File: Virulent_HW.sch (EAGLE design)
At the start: 28 parts

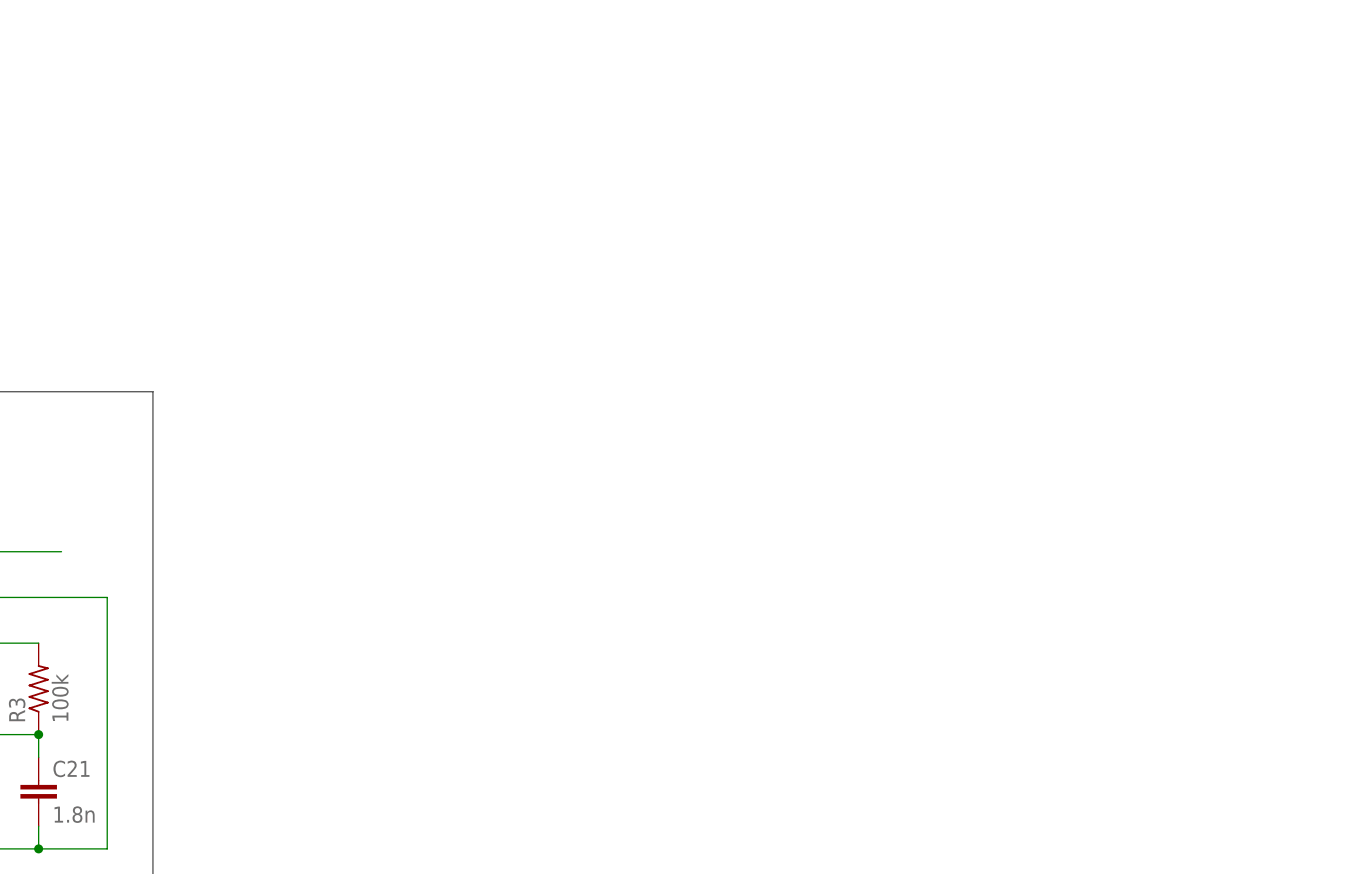
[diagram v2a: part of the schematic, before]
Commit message: Added crystal oscillator to library. Added carrier frequency circuitry to schematic.
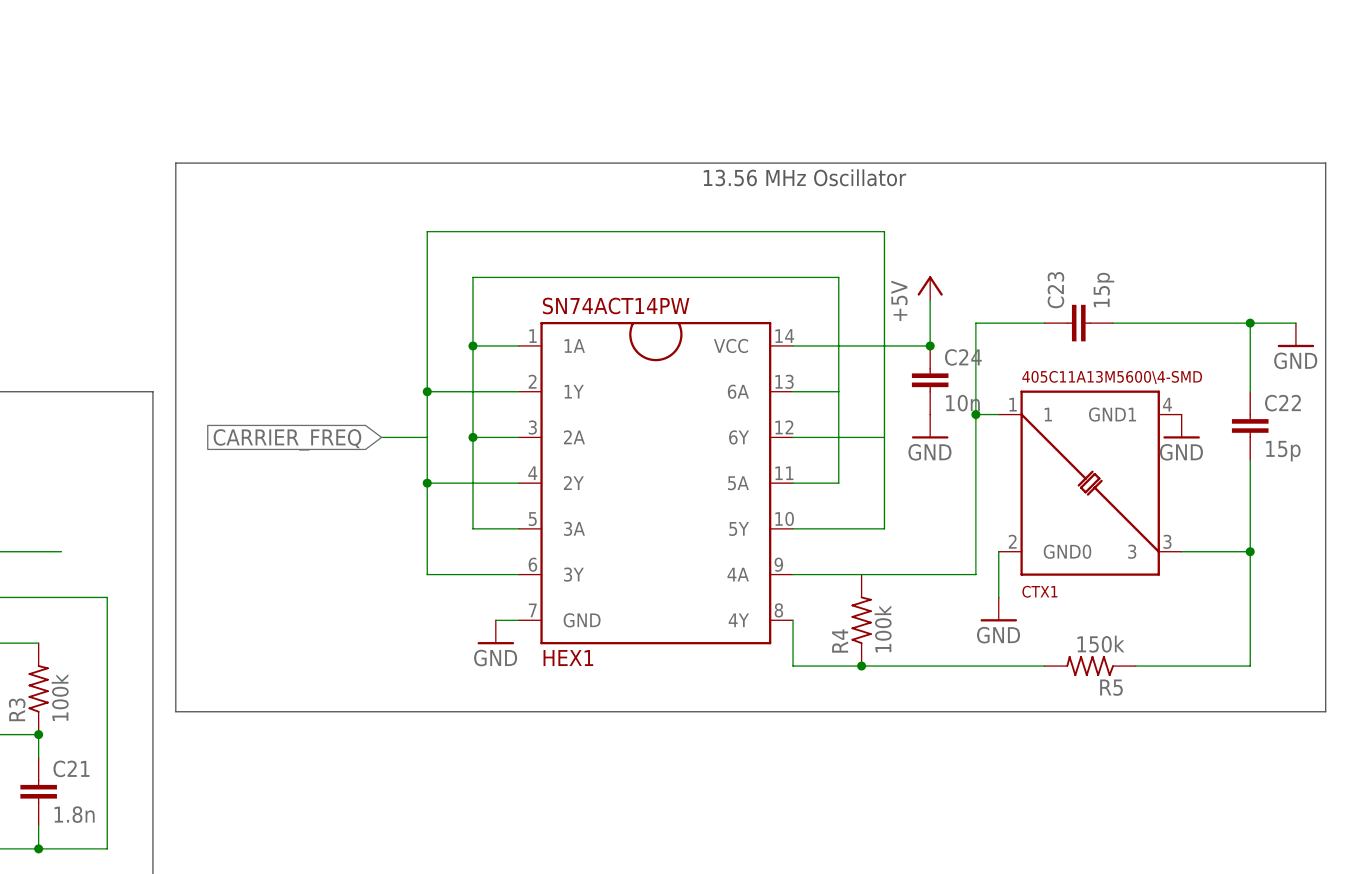
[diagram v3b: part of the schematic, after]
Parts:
- added C22, C23: 15p, rcl:C-EUC1206
- added C24: 10n, rcl:C-EUC1206
- added CTX1: 405C11A13M5600\4-SMD, Virulent_HW:405C11A13M5600\4-SMD
- added HEX1: SN74ACT14PW, Virulent_HW:SN74ACT14PW
- added R4: 100k, Virulent_HW:R-US_R0402
- added R5: 150k, Virulent_HW:R-US_R0402
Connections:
- new net CARRIER_FREQ: HEX1.1Y@2, HEX1.2Y@4, HEX1.3Y@6, HEX1.5Y@10, HEX1.6Y@12
- new net N$18: C23.1, CTX1.1@1, HEX1.4A@9, R4.2
- new net N$19: HEX1.4Y@8, R4.1, R5.2
- new net N$20: C22.2, CTX1.3@3, R5.1
- new net N$24: HEX1.1A@1, HEX1.2A@3, HEX1.3A@5, HEX1.5A@11, HEX1.6A@13
- net +5V: now also C24.1, HEX1.VCC@14
- net GND: now also C22.1, C23.2, C24.2, CTX1.GND0@2, CTX1.GND1@4, HEX1.GND@7
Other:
- note added: "13.56 MHz Oscillator"
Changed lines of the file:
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@@
 <part name="R3" library="Virulent_HW" deviceset="R-US_" device="R0402" value="100k"/>
 <part name="P+8" library="Virulent_HW" deviceset="+5V" device=""/>
+<part name="HEX1" library="Virulent_HW" deviceset="SN74ACT14" device="PW"/>
+<part name="CTX1" library="Virulent_HW" deviceset="405C11A13M5600" device="\4-SMD"/>
+<part name="GND9" library="Virulent_HW" deviceset="GND" device=""/>
+<part name="GND10" library="Virulent_HW" deviceset="GND" device=""/>
+<part name="R4" library="Virulent_HW" deviceset="R-US_" device="R0402" value="100k"/>
+<part name="R5" library="Virulent_HW" deviceset="R-US_" device="R0402" value="150k"/>
+<part name="C22" library="rcl" deviceset="C-EU" device="C1206" value="15p"/>
+<part name="C23" library="rcl" deviceset="C-EU" device="C1206" value="15p"/>
+<part name="GND11" library="Virulent_HW" deviceset="GND" device=""/>
+<part name="C24" library="rcl" deviceset="C-EU" device="C1206" value="10n"/>
+<part name="GND12" library="Virulent_HW" deviceset="GND" device=""/>
+<part name="P+9" library="Virulent_HW" deviceset="+5V" device=""/>
+<part name="GND13" library="Virulent_HW" deviceset="GND" device=""/>
 </parts>
 <sheets>
@@
 <wire x1="187.96" y1="71.12" x2="101.6" y2="71.12" width="0.1524" layer="97"/>
 <wire x1="101.6" y1="71.12" x2="101.6" y2="12.7" width="0.1524" layer="97"/>
+<wire x1="281.94" y1="96.52" x2="281.94" y2="35.56" width="0.1524" layer="97"/>
+<wire x1="281.94" y1="35.56" x2="409.702" y2="35.56" width="0.1524" layer="97"/>
+<wire x1="409.702" y1="35.56" x2="409.702" y2="96.52" width="0.1524" layer="97"/>
+<wire x1="409.702" y1="96.52" x2="281.94" y2="96.52" width="0.1524" layer="97"/>
+<text x="340.36" y="93.98" size="1.778" layer="97">13.56 MHz Oscillator</text>
 </plain>
 <instances>
@@
 <instance part="R3" gate="G$1" x="266.7" y="38.1" rot="R90"/>
 <instance part="P+8" gate="1" x="210.82" y="38.1" rot="R90"/>
+<instance part="HEX1" gate="G$1" x="335.28" y="60.96"/>
+<instance part="CTX1" gate="G$1" x="383.54" y="60.96"/>
+<instance part="GND9" gate="1" x="393.7" y="66.04"/>
+<instance part="GND10" gate="1" x="373.38" y="45.72"/>
+<instance part="R4" gate="G$1" x="358.14" y="45.72" rot="R90"/>
+<instance part="R5" gate="G$1" x="383.54" y="40.64" rot="R180"/>
+<instance part="C22" gate="G$1" x="401.32" y="68.58"/>
+<instance part="C23" gate="G$1" x="381" y="78.74" rot="R90"/>
+<instance part="GND11" gate="1" x="406.4" y="76.2"/>
+<instance part="C24" gate="G$1" x="365.76" y="73.66"/>
+<instance part="GND12" gate="1" x="365.76" y="66.04"/>
+<instance part="P+9" gate="1" x="365.76" y="83.82"/>
+<instance part="GND13" gate="1" x="317.5" y="43.18"/>
 </instances>
 <busses>
@@
 <wire x1="213.36" y1="38.1" x2="218.44" y2="38.1" width="0.1524" layer="91"/>
 <junction x="218.44" y="38.1"/>
+</segment>
+<segment>
+<pinref part="HEX1" gate="G$1" pin="VCC@14"/>
+<wire x1="350.52" y1="76.2" x2="365.76" y2="76.2" width="0.1524" layer="91"/>
+<wire x1="365.76" y1="76.2" x2="365.76" y2="81.28" width="0.1524" layer="91"/>
+<pinref part="C24" gate="G$1" pin="1"/>
+<junction x="365.76" y="76.2"/>
+<pinref part="P+9" gate="1" pin="+5V"/>
 </segment>
 </net>
@@
 <junction x="266.7" y="20.32"/>
 </segment>
+<segment>
+<pinref part="CTX1" gate="G$1" pin="GND1@4"/>
+<pinref part="GND9" gate="1" pin="GND"/>
+</segment>
+<segment>
+<pinref part="CTX1" gate="G$1" pin="GND0@2"/>
+<pinref part="GND10" gate="1" pin="GND"/>
+<wire x1="373.38" y1="48.26" x2="373.38" y2="53.34" width="0.1524" layer="91"/>
+</segment>
+<segment>
+<pinref part="C23" gate="G$1" pin="2"/>
+<wire x1="386.08" y1="78.74" x2="401.32" y2="78.74" width="0.1524" layer="91"/>
+<pinref part="C22" gate="G$1" pin="1"/>
+<wire x1="401.32" y1="78.74" x2="401.32" y2="71.12" width="0.1524" layer="91"/>
+<pinref part="GND11" gate="1" pin="GND"/>
+<wire x1="406.4" y1="78.74" x2="401.32" y2="78.74" width="0.1524" layer="91"/>
+<junction x="401.32" y="78.74"/>
+</segment>
+<segment>
+<pinref part="C24" gate="G$1" pin="2"/>
+<pinref part="GND12" gate="1" pin="GND"/>
+</segment>
+<segment>
+<pinref part="HEX1" gate="G$1" pin="GND@7"/>
+<wire x1="320.04" y1="45.72" x2="317.5" y2="45.72" width="0.1524" layer="91"/>
+<pinref part="GND13" gate="1" pin="GND"/>
+</segment>
 </net>
 <net name="5V_ENABLE" class="0">
@@
 </segment>
 </net>
+<net name="N$18" class="0">
+<segment>
+<pinref part="CTX1" gate="G$1" pin="1@1"/>
+<wire x1="370.84" y1="68.58" x2="373.38" y2="68.58" width="0.1524" layer="91"/>
+<wire x1="370.84" y1="68.58" x2="370.84" y2="78.74" width="0.1524" layer="91"/>
+<pinref part="C23" gate="G$1" pin="1"/>
+<wire x1="370.84" y1="78.74" x2="378.46" y2="78.74" width="0.1524" layer="91"/>
+<wire x1="370.84" y1="68.58" x2="370.84" y2="50.8" width="0.1524" layer="91"/>
+<pinref part="R4" gate="G$1" pin="2"/>
+<pinref part="HEX1" gate="G$1" pin="4A@9"/>
+<wire x1="350.52" y1="50.8" x2="358.14" y2="50.8" width="0.1524" layer="91"/>
+<wire x1="370.84" y1="50.8" x2="358.14" y2="50.8" width="0.1524" layer="91"/>
+<junction x="370.84" y="68.58"/>
+</segment>
+</net>
+<net name="N$19" class="0">
+<segment>
+<pinref part="R4" gate="G$1" pin="1"/>
+<wire x1="358.14" y1="40.64" x2="378.46" y2="40.64" width="0.1524" layer="91"/>
+<pinref part="R5" gate="G$1" pin="2"/>
+<junction x="358.14" y="40.64"/>
+<wire x1="358.14" y1="40.64" x2="350.52" y2="40.64" width="0.1524" layer="91"/>
+<pinref part="HEX1" gate="G$1" pin="4Y@8"/>
+<wire x1="350.52" y1="40.64" x2="350.52" y2="45.72" width="0.1524" layer="91"/>
+</segment>
+</net>
+<net name="N$20" class="0">
+<segment>
+<pinref part="R5" gate="G$1" pin="1"/>
+<wire x1="388.62" y1="40.64" x2="401.32" y2="40.64" width="0.1524" layer="91"/>
+<wire x1="401.32" y1="40.64" x2="401.32" y2="53.34" width="0.1524" layer="91"/>
+<pinref part="CTX1" gate="G$1" pin="3@3"/>
+<wire x1="401.32" y1="53.34" x2="393.7" y2="53.34" width="0.1524" layer="91"/>
+<pinref part="C22" gate="G$1" pin="2"/>
+<wire x1="401.32" y1="63.5" x2="401.32" y2="53.34" width="0.1524" layer="91"/>
+<junction x="401.32" y="53.34"/>
+</segment>
+</net>
+<net name="CARRIER_FREQ" class="0">
+<segment>
+<pinref part="HEX1" gate="G$1" pin="5Y@10"/>
+<wire x1="350.52" y1="55.88" x2="360.68" y2="55.88" width="0.1524" layer="91"/>
+<wire x1="360.68" y1="55.88" x2="360.68" y2="66.04" width="0.1524" layer="91"/>
+<pinref part="HEX1" gate="G$1" pin="6Y@12"/>
+<wire x1="360.68" y1="66.04" x2="350.52" y2="66.04" width="0.1524" layer="91"/>
+<wire x1="360.68" y1="66.04" x2="360.68" y2="88.9" width="0.1524" layer="91"/>
+<wire x1="360.68" y1="88.9" x2="309.88" y2="88.9" width="0.1524" layer="91"/>
+<pinref part="HEX1" gate="G$1" pin="3Y@6"/>
+<wire x1="320.04" y1="50.8" x2="309.88" y2="50.8" width="0.1524" layer="91"/>
+<wire x1="309.88" y1="50.8" x2="309.88" y2="60.96" width="0.1524" layer="91"/>
+<pinref part="HEX1" gate="G$1" pin="1Y@2"/>
+<wire x1="309.88" y1="60.96" x2="309.88" y2="66.04" width="0.1524" layer="91"/>
+<wire x1="309.88" y1="66.04" x2="309.88" y2="71.12" width="0.1524" layer="91"/>
+<wire x1="309.88" y1="71.12" x2="320.04" y2="71.12" width="0.1524" layer="91"/>
+<pinref part="HEX1" gate="G$1" pin="2Y@4"/>
+<wire x1="320.04" y1="60.96" x2="309.88" y2="60.96" width="0.1524" layer="91"/>
+<junction x="309.88" y="60.96"/>
+<wire x1="309.88" y1="88.9" x2="309.88" y2="71.12" width="0.1524" layer="91"/>
+<junction x="309.88" y="71.12"/>
+<wire x1="309.88" y1="66.04" x2="304.8" y2="66.04" width="0.1524" layer="91"/>
+<label x="304.8" y="66.04" size="1.778" layer="95" rot="R180" xref="yes"/>
+</segment>
+</net>
+<net name="N$24" class="0">
+<segment>
+<pinref part="HEX1" gate="G$1" pin="5A@11"/>
+<wire x1="350.52" y1="60.96" x2="355.6" y2="60.96" width="0.1524" layer="91"/>
+<wire x1="355.6" y1="60.96" x2="355.6" y2="71.12" width="0.1524" layer="91"/>
+<pinref part="HEX1" gate="G$1" pin="6A@13"/>
+<wire x1="355.6" y1="71.12" x2="350.52" y2="71.12" width="0.1524" layer="91"/>
+<wire x1="355.6" y1="71.12" x2="355.6" y2="83.82" width="0.1524" layer="91"/>
+<wire x1="355.6" y1="83.82" x2="314.96" y2="83.82" width="0.1524" layer="91"/>
+<pinref part="HEX1" gate="G$1" pin="3A@5"/>
+<wire x1="320.04" y1="55.88" x2="314.96" y2="55.88" width="0.1524" layer="91"/>
+<wire x1="314.96" y1="55.88" x2="314.96" y2="66.04" width="0.1524" layer="91"/>
+<pinref part="HEX1" gate="G$1" pin="1A@1"/>
+<wire x1="314.96" y1="66.04" x2="314.96" y2="76.2" width="0.1524" layer="91"/>
+<wire x1="314.96" y1="76.2" x2="320.04" y2="76.2" width="0.1524" layer="91"/>
+<pinref part="HEX1" gate="G$1" pin="2A@3"/>
+<wire x1="320.04" y1="66.04" x2="314.96" y2="66.04" width="0.1524" layer="91"/>
+<junction x="314.96" y="66.04"/>
+<wire x1="314.96" y1="83.82" x2="314.96" y2="76.2" width="0.1524" layer="91"/>
+<junction x="314.96" y="76.2"/>
+</segment>
+</net>

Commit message: Added uC and LED to schematic.
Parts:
- added R10, R11, R12, R13, R6, R7, R8, R9: 10k, Virulent_HW:R-US_R0402
- added RGB1: MSL0201RGBW15, Virulent_HW:MSL0201RGBW15
- added U1: STM32F050G6U6, Virulent_HW:STM32F050G6U6
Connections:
- new net N$11: R11.1, RGB1.G@1
- new net N$16: R13.1, RGB1.B@3
- new net N$21: R11.2, U1IO.PB1@15
- new net N$22: R12.2, U1IO.PB3@24
- new net N$23: R13.2, U1IO.PB4@25
- new net PLL_INT2: PLL1.OUPUT@8, R6.1, U1IO.PA0@6
- new net PLL_INT3: PLL2.OUPUT@8, R7.1, U1IO.PB0@14
- new net PLL_INT5: PLL3.OUPUT@8, R8.1, U1IO.PF0/OSC_IN@2
- net +3.3V: now also R10.2, R6.2, R7.2, R8.2, RGB1.V+@4, U1PWR/CTRL.VDD@17, U1PWR/CTRL.VDDA@5
- net 5V_ENABLE: now also U1IO.PA1@7
- net GND: now also R9.1, U1PWR/CTRL.VSS@16
- net N$15: now also R12.1, RGB1.R@2; no longer PLL3.OUPUT@8
- net N$6: now also R10.1, U1PWR/CTRL.NRST@4; no longer PLL1.OUPUT@8
- net N$9: now also R9.2, U1PWR/CTRL.BOOT0@1; no longer PLL2.OUPUT@8
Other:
- note added: "Pinout for IO is temporary"
- moved on the sheet: C10, C11, C12, C9
